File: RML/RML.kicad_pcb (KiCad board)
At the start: 2 copper layers, 4 parts, among them U1 LR8K4-G, U101 LMC555xM, U102 641964-1, U3 SFH617A-1

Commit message: RML footprints
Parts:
- removed U101: LMC555xM, Package_SO:SOIC-8_3.9x4.9mm_P1.27mm
- added C1: 0.33uF, Capacitor_SMD:C_0402_1005Metric, F.Cu at (79.5, 69.5)
- added C101: 1u, Capacitor_SMD:C_0201_0603Metric, F.Cu at (46.5, 107.5)
- added C102: 0.1u, Capacitor_SMD:C_0402_1005Metric, F.Cu at (33.0, 98.5)
- added C103: .01u, Capacitor_SMD:C_0402_1005Metric, F.Cu at (84.0, 73.5)
- added C105: 22u, Capacitor_SMD:C_0402_1005Metric, F.Cu at (52.5, 103.5)
- added C2: 0.01uF, Capacitor_SMD:C_0402_1005Metric, F.Cu at (29.5, 107.5)
- added Q1: NMOS, Package_TO_SOT_THT:TO-220-3_Vertical, F.Cu at (117.5, 82.0)
- added R102: 10k, Capacitor_SMD:C_0402_1005Metric, F.Cu at (94.0, 93.0)
- added R105: 15k, Capacitor_SMD:C_0402_1005Metric, F.Cu at (39.0, 112.0)
- added R106: 100k, Capacitor_SMD:C_0402_1005Metric, F.Cu at (47.0, 100.5)
- added R2: 100k, Capacitor_SMD:C_0402_1005Metric, F.Cu at (107.5, 81.5)
- added R3: 4.7k, Resistor_SMD:R_2512_6332Metric_Pad1.40x3.35mm_HandSolder, F.Cu at (33.0, 89.5)
- added R4: 4.7k, Resistor_SMD:R_2512_6332Metric_Pad1.40x3.35mm_HandSolder, F.Cu at (42.0, 89.5)
- added R5: 4.7k, Resistor_SMD:R_2512_6332Metric_Pad1.40x3.35mm_HandSolder, F.Cu at (51.0, 89.5)
- added R6: 4.7k, Resistor_SMD:R_2512_6332Metric_Pad1.40x3.35mm_HandSolder, F.Cu at (60.0, 89.5)
- added R7: 4.7k, Resistor_SMD:R_2512_6332Metric_Pad1.40x3.35mm_HandSolder, F.Cu at (69.0, 89.5)
- added R8: 4.7k, Resistor_SMD:R_2512_6332Metric_Pad1.40x3.35mm_HandSolder, F.Cu at (78.0, 89.5)
- added U103: 641964-1, CONNECTOR:641964-1_TYC, F.Cu at (22.0, 94.3)
- added U104: LM555xM, Package_SO:SOIC-8_3.9x4.9mm_P1.27mm, F.Cu at (38.5, 104.4)
- added U2: LM7805_TO220, Package_TO_SOT_THT:TO-220-3_Vertical, F.Cu at (89.9, 80.0)
- U1: value LR8K4-G -> 74AHC1G02; footprint Package_TO_SOT_SMD:TO-252-2 -> Package_TO_SOT_SMD:SOT-23-5
- moved U102 104.0 mm to (118.0, 104.8), turned to 90 degrees
- moved U1 79.0 mm to (101.9, 94.5)
- moved U3 64.3 mm to (82.7, 96.2)
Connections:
- U1 pad 1: Net-(D1-K) -> Net-(R102-Pad2)
- U1 pad 2: Net-(D1-A) -> CLOCK
- U1 pad 3: Net-(U1-ADJ) -> GND
- U102 pad 1: unconnected-(U102-Pad1) -> Net-(Q1-S)
- U102 pad 2: unconnected-(U102-Pad2) -> GND
- U3 pad 1: Net-(D1-A) -> 12.5 mA
- U3 pad 2: Net-(R101-Pad1) -> GNDPWR
- U3 pad 3: Net-(R6-Pad1) -> GND
- U3 pad 4: Net-(D101-A2) -> Net-(R102-Pad2)

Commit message: Broken pcb
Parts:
- moved U104 17.7 mm to (55.5, 99.5)
- moved C103 17.1 mm to (100.5, 78.0)
- moved R105 16.7 mm to (49.5, 99.0)
- moved R106 15.1 mm to (62.0, 98.5), turned to 90 degrees
- moved C2 14.0 mm to (41.0, 99.5), turned to 90 degrees
- moved C1 13.2 mm to (91.0, 76.0)
- moved C105 9.51 mm to (62.0, 103.0), turned to 90 degrees
- moved C101 8.06 mm to (45.5, 99.5), turned to 90 degrees
- moved R102 7.44 mm to (87.0, 90.5)
- moved C102 4.12 mm to (37.0, 99.5), turned to 90 degrees
- moved U1 3.07 mm to (101.5, 97.5)
- moved U2 2.95 mm to (90.0, 82.9)
- moved U3 2.50 mm to (85.2, 96.2)
- turned R3 to 180 degrees
- turned R4 to 180 degrees
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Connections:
- C101 pad 1: Net-(U104-R) -> +5V
- C102 pad 1: Net-(U104-R) -> +5V
- C2 pad 1: Net-(U1-VCC) -> +5V
- R106 pad 2: Net-(U104-R) -> +5V
- R8 pad 1: 12.5mA -> 12.5 mA
- U1 pad 5: Net-(U1-VCC) -> +5V
- U104 pad 4: Net-(U104-R) -> +5V
- U104 pad 8: Net-(U104-R) -> +5V
- U2 pad 3: Net-(U1-VCC) -> +5V
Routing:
- net GND: track 0.00 -> 130.6 mm, vias 0 -> 2
- net +5V: track 0.00 -> 73.0 mm, vias 0 -> 2
- net GNDPWR: track 0.00 -> 68.1 mm
- net Net-(R102-Pad2): track 0.00 -> 19.0 mm
- net +12V: track 0.00 -> 16.6 mm
- net /THRESH: track 0.00 -> 11.6 mm
- net 352.8V: track 0.00 -> 9.93 mm
- net 12.5 mA: track 0.00 -> 9.64 mm
- net CLOCK: track 0.00 -> 4.48 mm
- net Net-(R6-Pad1): track 0.00 -> 2.95 mm
- net Net-(R4-Pad1): track 0.00 -> 2.90 mm
- net Net-(R3-Pad1): track 0.00 -> 2.90 mm
- net Net-(R7-Pad1): track 0.00 -> 2.85 mm
- net Net-(R5-Pad1): track 0.00 -> 2.85 mm

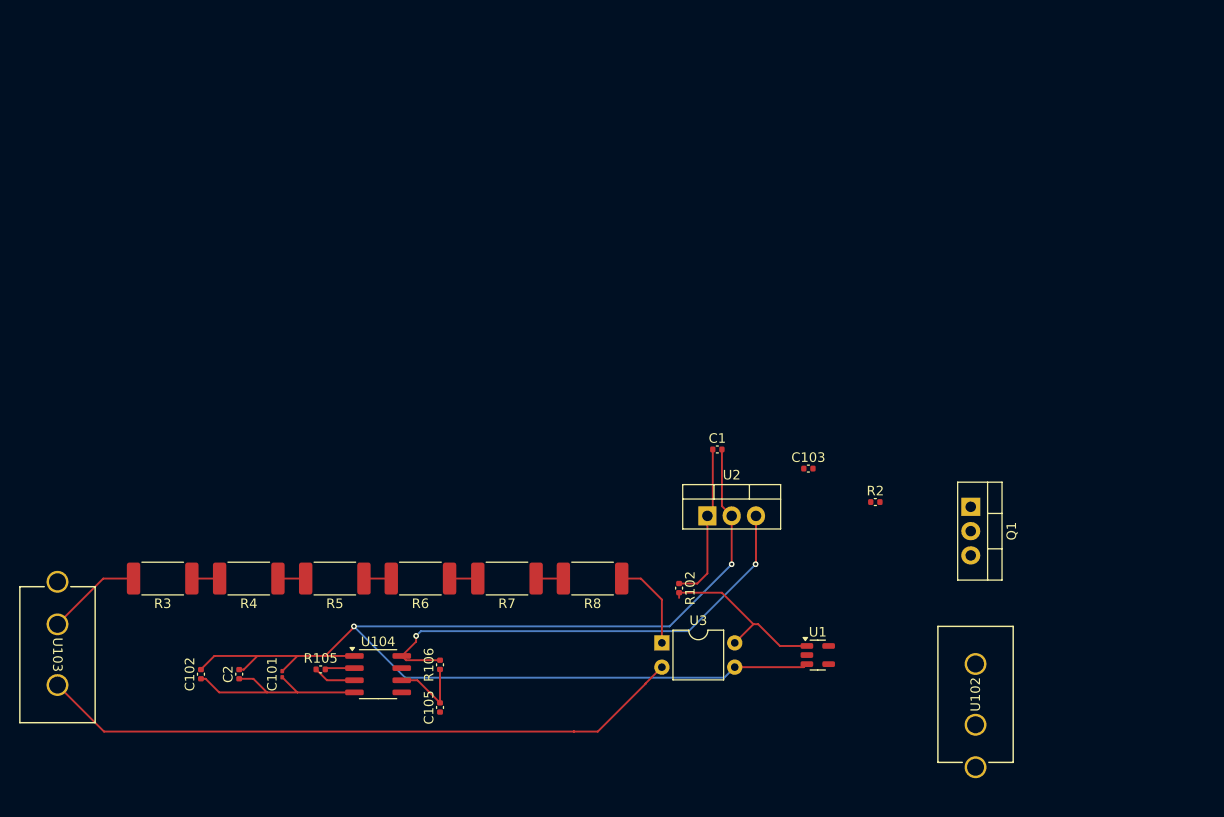
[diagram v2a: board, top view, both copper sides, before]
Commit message: Not correct footprints...need to change later.
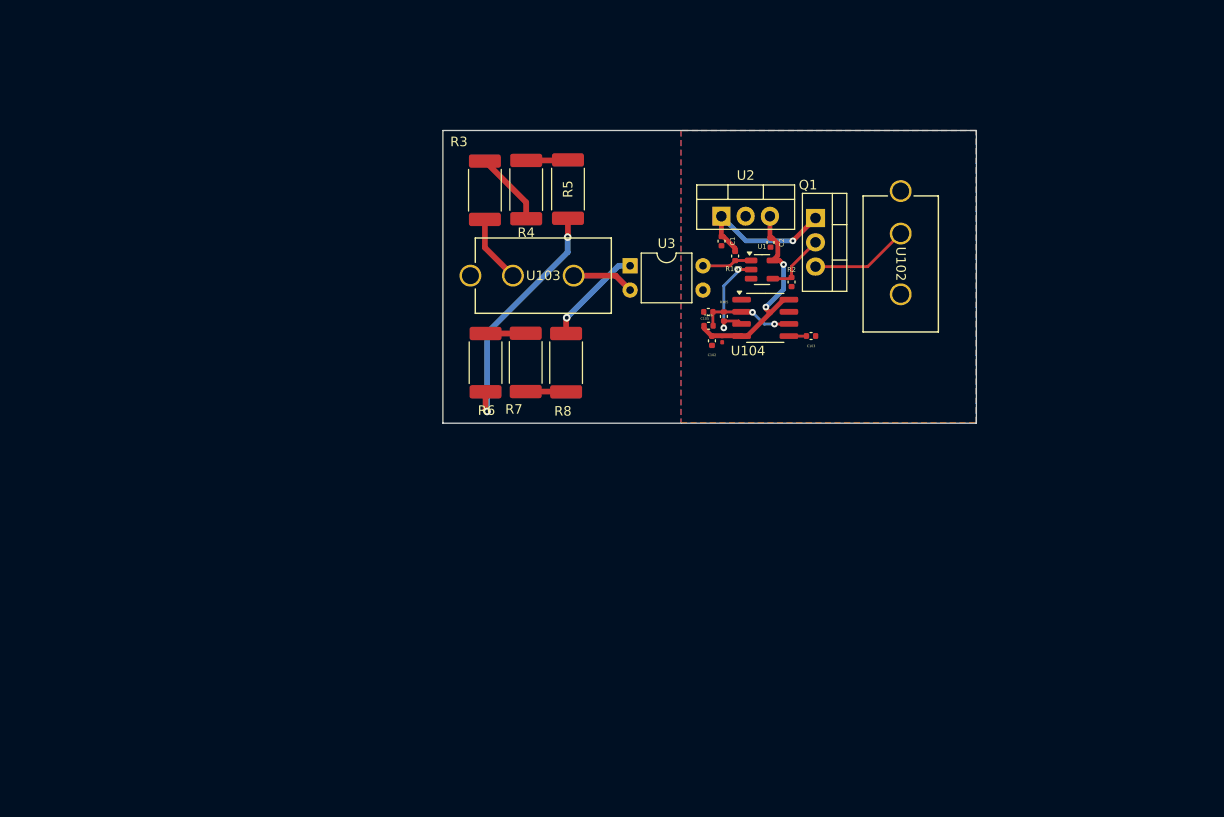
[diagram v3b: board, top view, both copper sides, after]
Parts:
- moved C2 71.6 mm to (96.6, 54.4), turned to -90 degrees
- moved C102 63.8 mm to (90.4, 64.6), turned to -90 degrees
- moved U103 60.0 mm to (69.6, 57.8), turned to 0 degrees
- moved C101 57.8 mm to (91.5, 64.5), turned to -90 degrees
- moved R105 56.0 mm to (91.7, 62.1), turned to 90 degrees
- moved U104 55.0 mm to (96.0, 62.2)
- moved R3 52.8 mm to (66.7, 48.9), turned to -90 degrees
- moved U102 52.0 mm to (110.2, 53.4), turned to -90 degrees
- moved C105 50.0 mm to (90.1, 61.6), turned to 0 degrees
- moved R4 50.0 mm to (71.0, 48.8), turned to -90 degrees
- moved R5 47.5 mm to (75.4, 48.8), turned to 90 degrees
- moved R106 45.2 mm to (90.1, 63.1), turned to 180 degrees
- moved U1 40.7 mm to (95.7, 57.2)
- moved U3 39.6 mm to (81.9, 56.8)
- moved R102 35.2 mm to (92.9, 55.8)
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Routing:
- net GND: track 130.6 -> 0.00 mm, vias 2 -> 0
- net GNDPWR: track 68.1 -> 6.53 mm
- net +5V: track 73.0 -> 23.7 mm
- net Net-(R5-Pad1): track 2.85 -> 26.1 mm, vias 0 -> 2
- net Net-(R102-Pad2): track 19.0 -> 5.26 mm
- net Net-(Q1-S): track 0.00 -> 10.7 mm
- net Net-(Q1-G): track 0.00 -> 6.72 mm
- net CLOCK: track 4.48 -> 10.8 mm, vias 0 -> 2
- net Net-(R3-Pad1): track 2.90 -> 7.82 mm
- net 352.8V: track 9.93 -> 7.10 mm
- net Net-(U104-CV): track 0.00 -> 1.84 mm
- net /THRESH: track 11.6 -> 9.95 mm, vias 0 -> 2
- net Net-(R4-Pad1): track 2.90 -> 4.39 mm
- net Net-(R7-Pad1): track 2.85 -> 4.23 mm
- net 12.5 mA: track 9.64 -> 10.9 mm, vias 0 -> 1
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- added copper zone on B.Cu, net GND
- added copper zone on F.Cu, net GND
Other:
- board outline added: 55.8 x 30.6 mm

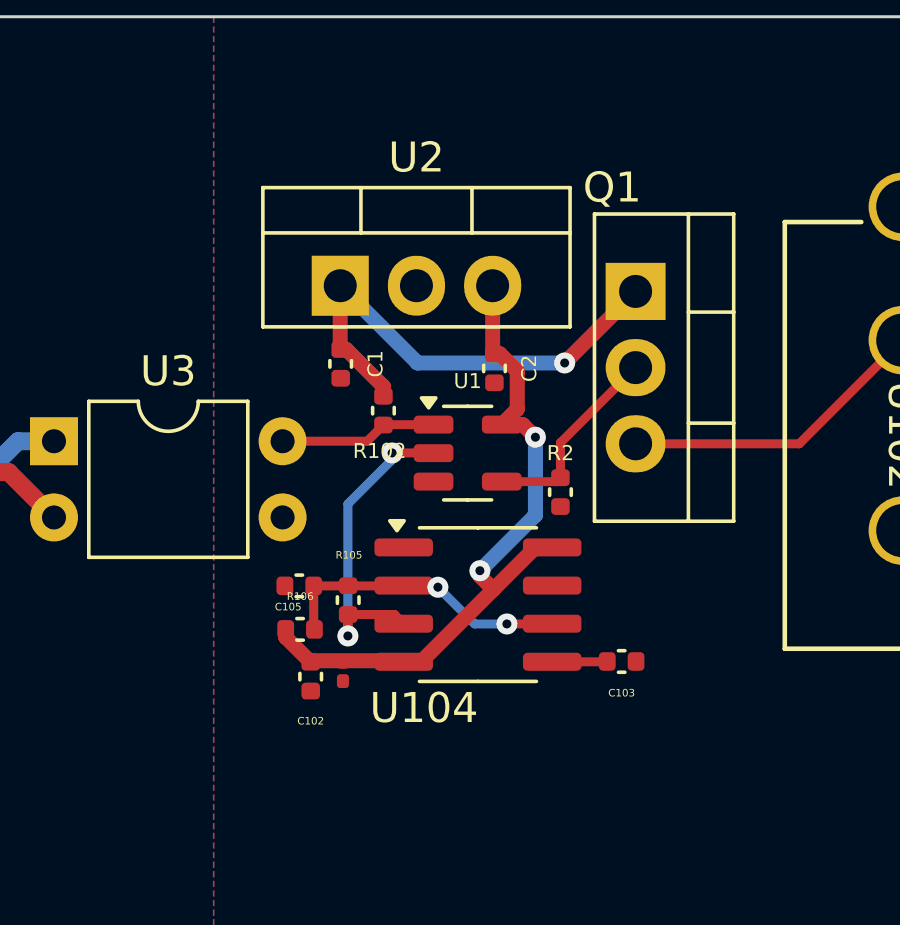
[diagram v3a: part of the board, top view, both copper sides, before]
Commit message: minor updates to fault latch and RML pcb layout
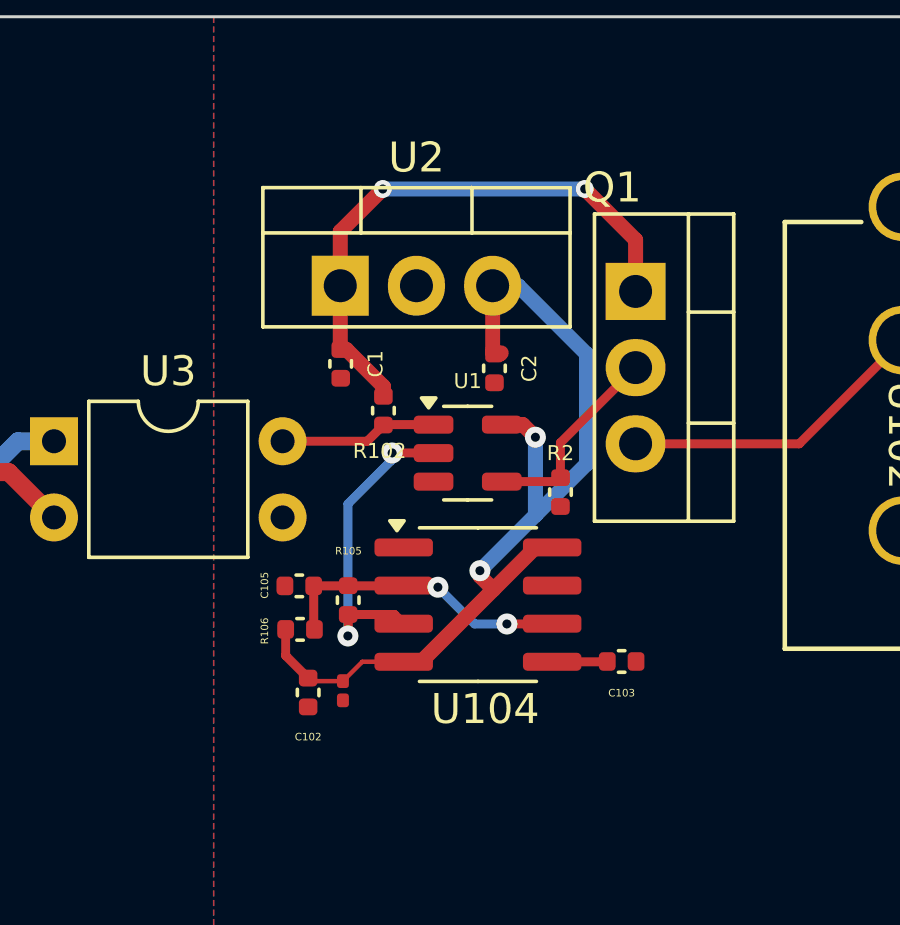
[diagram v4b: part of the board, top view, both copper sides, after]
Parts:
- moved C101 0.64 mm to (91.5, 65.1)
- moved C102 0.54 mm to (90.3, 65.2)
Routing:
- net +5V: track 23.7 -> 32.0 mm
- net +12V: track 16.3 -> 19.1 mm, vias 1 -> 2
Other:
- copper layers 2 -> 4
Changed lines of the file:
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@@
 	(generator_version "9.0")
 	(general
-		(thickness 1.6)
+		(thickness 1.600198)
 		(legacy_teardrops no)
 	)
@@
 	(layers
 		(0 "F.Cu" signal)
+		(4 "In1.Cu" signal)
+		(6 "In2.Cu" signal)
 		(2 "B.Cu" signal)
-		(9 "F.Adhes" user "F.Adhesive")
-		(11 "B.Adhes" user "B.Adhesive")
 		(13 "F.Paste" user)
 		(15 "B.Paste" user)
@@
 		(1 "F.Mask" user)
 		(3 "B.Mask" user)
-		(17 "Dwgs.User" user "User.Drawings")
-		(19 "Cmts.User" user "User.Comments")
-		(21 "Eco1.User" user "User.Eco1")
-		(23 "Eco2.User" user "User.Eco2")
 		(25 "Edge.Cuts" user)
 		(27 "Margin" user)
@@
 		(29 "B.CrtYd" user "B.Courtyard")
 		(35 "F.Fab" user)
-		(33 "B.Fab" user)
-		(39 "User.1" user)
-		(41 "User.2" user)
-		(43 "User.3" user)
-		(45 "User.4" user)
-		(47 "User.5" user)
-		(49 "User.6" user)
-		(51 "User.7" user)
-		(53 "User.8" user)
-		(55 "User.9" user)
 	)
 	(setup
@@
 			(layer "dielectric 1"
 				(type "core")
-				(thickness 1.51)
+				(thickness 0.480066)
+				(material "FR4")
+				(epsilon_r 4.5)
+				(loss_tangent 0.02)
+			)
+			(layer "In1.Cu"
+				(type "copper")
+				(thickness 0.035)
+			)
+			(layer "dielectric 2"
+				(type "prepreg")
+				(thickness 0.480066)
+				(material "FR4")
+				(epsilon_r 4.5)
+				(loss_tangent 0.02)
+			)
+			(layer "In2.Cu"
+				(type "copper")
+				(thickness 0.035)
+			)
+			(layer "dielectric 3"
+				(type "core")
+				(thickness 0.480066)
 				(material "FR4")
 				(epsilon_r 4.5)
@@
 		)
 		(pad_to_mask_clearance 0)
+		(solder_mask_min_width 0.12)
 		(allow_soldermask_bridges_in_footprints no)
 		(tenting front back)
@@
 	(footprint "Capacitor_SMD:C_0402_1005Metric"
 		(layer "F.Cu")
-		(at 90.435 64.641 -90)
+		(at 90.35 65.17 -90)
 		(descr "Capacitor SMD 0402 (1005 Metric), square (rectangular) end terminal, IPC_7351 nominal, (Body size source: IPC-SM-782 page 76, https://www.pcb-3d.com/wordpress/wp-content/uploads/ipc-sm-782a_amendment_1_and_2.pdf), generated with kicad-footprint-generator")
 		(tags "capacitor")
@@
 		(tags "capacitor")
 		(property "Reference" "R105"
-			(at 1.5 0.025 180)
+			(at 1.639 0.009 0)
 			(layer "F.SilkS")
 			(effects
@@
 	(footprint "Capacitor_SMD:C_0201_0603Metric"
 		(layer "F.Cu")
-		(at 91.51 64.471 -90)
+		(at 91.51 65.111 -90)
 		(descr "Capacitor SMD 0201 (0603 Metric), square (rectangular) end terminal, IPC_7351 nominal, (Body size source: https://www.vishay.com/docs/20052/crcw0201e3.pdf), generated with kicad-footprint-generator")
 		(tags "capacitor")
@@
 		)
 		(property "Value" "1u"
-			(at 0.895 0 180)
+			(at 0.895 0 0)
 			(layer "F.Fab")
 			(effects
@@
 		(tags "capacitor")
 		(property "Reference" "C105"
-			(at -0.37 0.7 0)
+			(at -1.155 -0.021 90)
 			(layer "F.SilkS")
 			(effects
@@
 		(tags "capacitor")
 		(property "Reference" "R106"
-			(at -0.005 1.1 0)
+			(at 1.18 -0.053 90)
 			(layer "F.SilkS")
 			(effects
@@
 		(tags "SOIC SO")
 		(property "Reference" "U104"
-			(at -1.8 3.45 0)
+			(at 0.24 3.484 0)
 			(layer "F.SilkS")
 			(effects
@@
 		)
 		(property "Value" "LM555xM"
-			(at -0.325 4.925 0)
+			(at 0.54 4.909 0)
 			(layer "F.Fab")
 			(effects
@@
 	)
 	(segment
-		(start 101.265 51.821)
-		(end 98.9 54.186)
+		(start 91.42 51.611)
+		(end 91.42 49.804)
 		(width 0.5)
 		(layer "F.Cu")
@@
 	)
 	(segment
+		(start 101.265 50.084)
+		(end 101.265 51.801)
+		(width 0.5)
+		(layer "F.Cu")
+		(net 2)
+	)
+	(segment
 		(start 91.42 53.721)
 		(end 91.435 53.736)
@@
 	)
 	(segment
+		(start 91.42 49.804)
+		(end 92.837 48.387)
+		(width 0.5)
+		(layer "F.Cu")
+		(net 2)
+	)
+	(segment
+		(start 99.568 48.387)
+		(end 101.265 50.084)
+		(width 0.5)
+		(layer "F.Cu")
+		(net 2)
+	)
+	(segment
 		(start 91.625 53.736)
 		(end 92.859 54.97)
@@
 	)
 	(via
-		(at 98.9 54.186)
-		(size 0.7)
+		(at 99.568 48.387)
+		(size 0.6)
 		(drill 0.3)
 		(layers "F.Cu" "B.Cu")
 		(net 2)
 	)
-	(segment
-		(start 98.9 54.186)
-		(end 93.995 54.186)
-		(width 0.5)
-		(layer "B.Cu")
+	(via
+		(at 92.837 48.387)
+		(size 0.6)
+		(drill 0.3)
+		(layers "F.Cu" "B.Cu")
 		(net 2)
 	)
 	(segment
-		(start 93.995 54.186)
-		(end 91.42 51.611)
+		(start 92.837 48.387)
+		(end 99.568 48.387)
 		(width 0.5)
 		(layer "B.Cu")
@@
 	)
 	(segment
-		(start 96.5 53.826)
-		(end 96.56 53.886)
-		(width 0.5)
+		(start 89.6 63.94)
+		(end 89.6 63.066)
+		(width 0.3)
 		(layer "F.Cu")
 		(net 4)
 	)
 	(segment
-		(start 90.486 64.11)
-		(end 93.499 64.11)
+		(start 96.5 53.826)
+		(end 96.56 53.886)
 		(width 0.5)
 		(layer "F.Cu")
@@
 	)
 	(segment
-		(start 97.321 54.457318)
-		(end 97.321 55.725)
+		(start 97.9259 60.336)
+		(end 98.485 60.336)
 		(width 0.5)
 		(layer "F.Cu")
@@
 	)
 	(segment
-		(start 97.9259 60.336)
-		(end 98.485 60.336)
+		(start 96.5 51.611)
+		(end 96.5 53.826)
 		(width 0.5)
 		(layer "F.Cu")
@@
 	)
 	(segment
-		(start 96.56 53.886)
-		(end 96.749682 53.886)
+		(start 97.505 56.241)
+		(end 97.925 56.661)
 		(width 0.5)
 		(layer "F.Cu")
@@
 	)
 	(segment
-		(start 96.5 51.611)
-		(end 96.5 53.826)
+		(start 96.749682 53.886)
+		(end 96.785682 53.85)
 		(width 0.5)
 		(layer "F.Cu")
@@
 	)
 	(segment
-		(start 90.435 64.161)
-		(end 89.6 63.326)
+		(start 94.1159 64.146)
+		(end 96.52545 61.73645)
 		(width 0.5)
 		(layer "F.Cu")
@@
 	)
 	(segment
-		(start 96.749682 53.886)
-		(end 97.321 54.457318)
-		(width 0.5)
+		(start 93.535 64.146)
+		(end 92.155 64.146)
+		(width 0.15)
 		(layer "F.Cu")
 		(net 4)
 	)
 	(segment
-		(start 97.505 56.241)
-		(end 97.925 56.661)
+		(start 93.499 64.11)
+		(end 93.535 64.146)
 		(width 0.5)
 		(layer "F.Cu")
@@
 	)
 	(segment
-		(start 94.1159 64.146)
-		(end 96.52545 61.73645)
+		(start 96.56 53.886)
+		(end 96.749682 53.886)
 		(width 0.5)
 		(layer "F.Cu")
@@
 	)
 	(segment
-		(start 93.499 64.11)
-		(end 93.535 64.146)
-		(width 0.5)
+		(start 91.51 64.791)
+		(end 90.451 64.791)
+		(width 0.15)
 		(layer "F.Cu")
 		(net 4)
 	)
 	(segment
-		(start 90.435 64.161)
-		(end 90.486 64.11)
-		(width 0.5)
+		(start 90.35 64.69)
+		(end 89.6 63.94)
+		(width 0.3)
 		(layer "F.Cu")
 		(net 4)
 	)
 	(segment
-		(start 93.535 64.146)
-		(end 94.1159 64.146)
-		(width 0.5)
+		(start 90.451 64.791)
+		(end 90.35 64.69)
+		(width 0.15)
 		(layer "F.Cu")
 		(net 4)
 	)
 	(segment
-		(start 97.321 55.725)
-		(end 96.805 56.241)
+		(start 93.535 64.146)
+		(end 94.1159 64.146)
 		(width 0.5)
 		(layer "F.Cu")
@@
 	)
 	(segment
-		(start 89.6 63.326)
-		(end 89.6 63.066)
-		(width 0.5)
+		(start 92.155 64.146)
+		(end 91.51 64.791)
+		(width 0.15)
 		(layer "F.Cu")
 		(net 4)
@@
 		(width 0.5)
 		(layer "B.Cu")
+		(net 4)
+	)
+	(segment
+		(start 99.628 57.558)
+		(end 99.628 53.884452)
+		(width 0.5)
+		(layer "B.Cu")
+		(net 4)
+	)
+	(segment
+		(start 97.925 59.261)
+		(end 99.628 57.558)
+		(width 0.5)
+		(layer "B.Cu")
+		(net 4)
+	)
+	(segment
+		(start 99.628 53.884452)
+		(end 97.354548 51.611)
+		(width 0.5)
+		(layer "B.Cu")
+		(net 4)
+	)
+	(segment
+		(start 97.354548 51.611)
+		(end 96.5 51.611)
+		(width 0.5)
+		(layer "B.Cu")
